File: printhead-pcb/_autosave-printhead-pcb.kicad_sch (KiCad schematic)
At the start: 25 parts, among them J1 Power, J3 DATA, U1 PCA9615DP, U6 AP7361C-33E

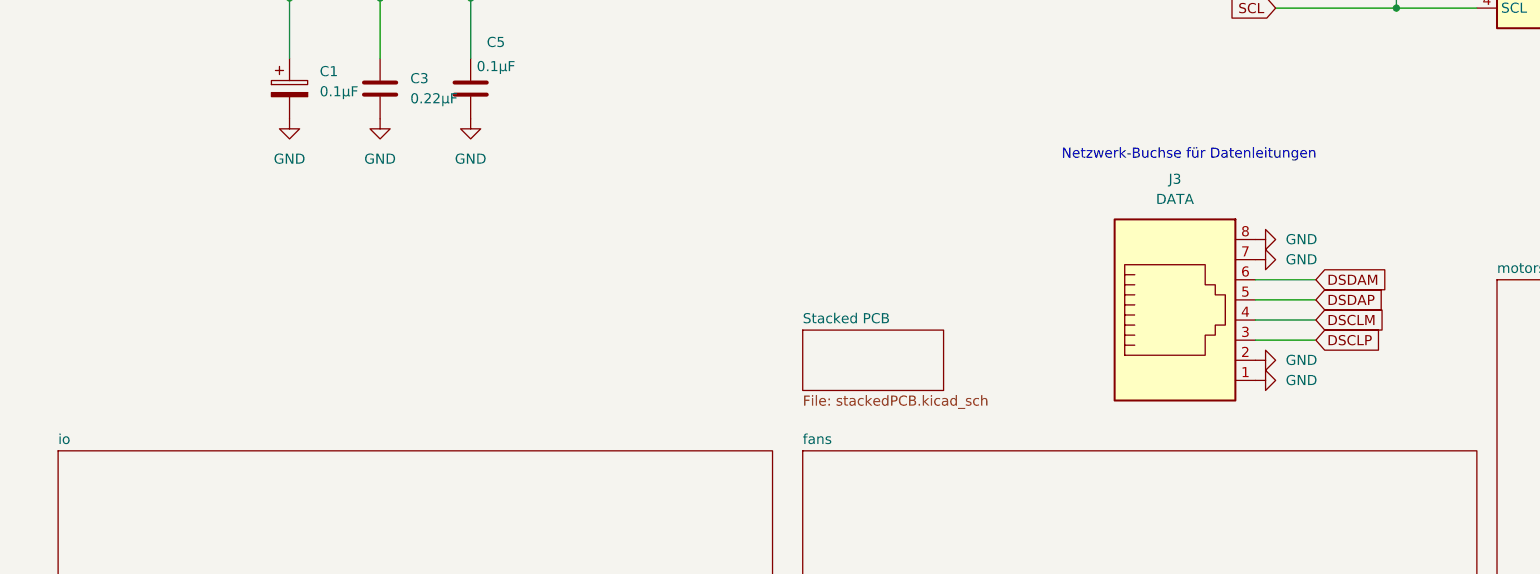
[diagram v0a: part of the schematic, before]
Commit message: made first pcb design of module 1 with components on front and back
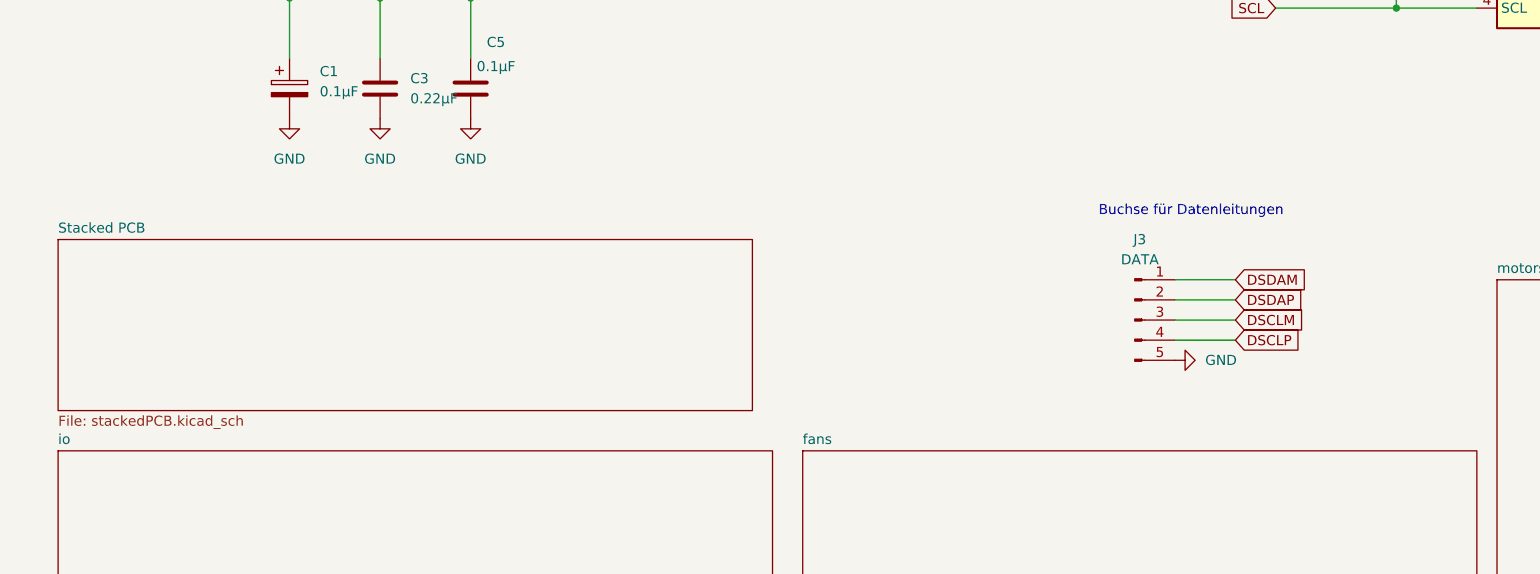
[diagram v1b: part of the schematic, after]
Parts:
- removed J3: DATA, Connector_RJ:RJ45_Molex_0855135013_Vertical, symbol Connector:RJ45
- added J3: DATA, Connector_PinHeader_2.54mm:PinHeader_1x05_P2.54mm_Horizontal, symbol Connector:Conn_01x05_Pin
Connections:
- net DSCLM: now also J3.3 (Pin_3)
- net DSCLP: now also J3.4 (Pin_4)
- net DSDAM: now also J3.1 (Pin_1)
- net DSDAP: now also J3.2 (Pin_2)
- net GND: now also J3.5 (Pin_5)
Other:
- note added: "Buchse für Datenleitungen"
- note removed: "Netzwerk-Buchse für Datenleitungen"
